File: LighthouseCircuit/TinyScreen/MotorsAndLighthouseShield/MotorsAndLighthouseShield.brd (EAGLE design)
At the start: 21.6 x 19.1 mm, 29 parts

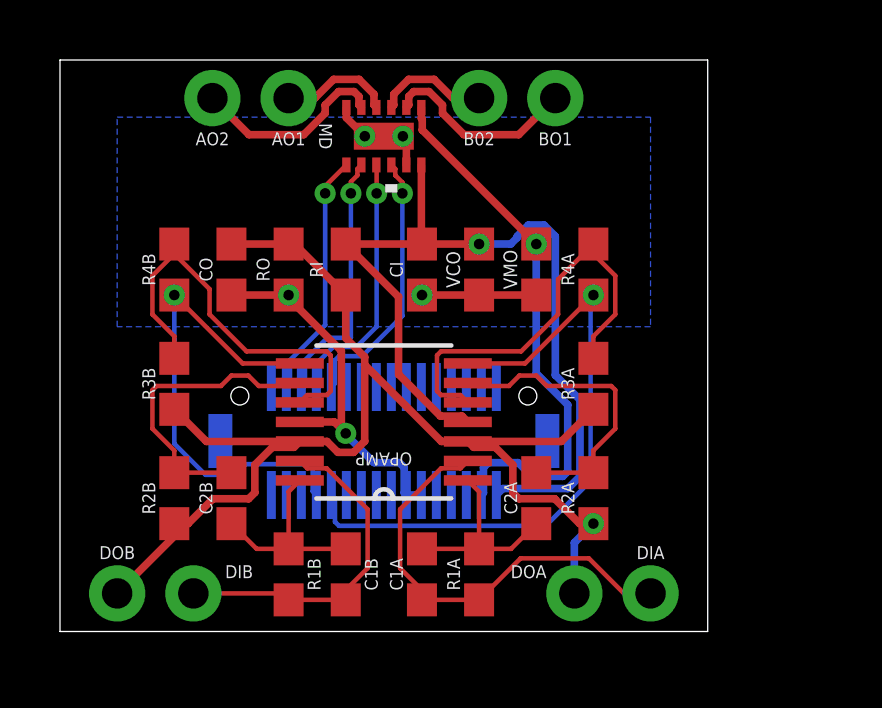
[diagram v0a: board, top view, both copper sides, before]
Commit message: Significantly stabilized the position calculation and the new driving model with independent PIDs for each wheel.
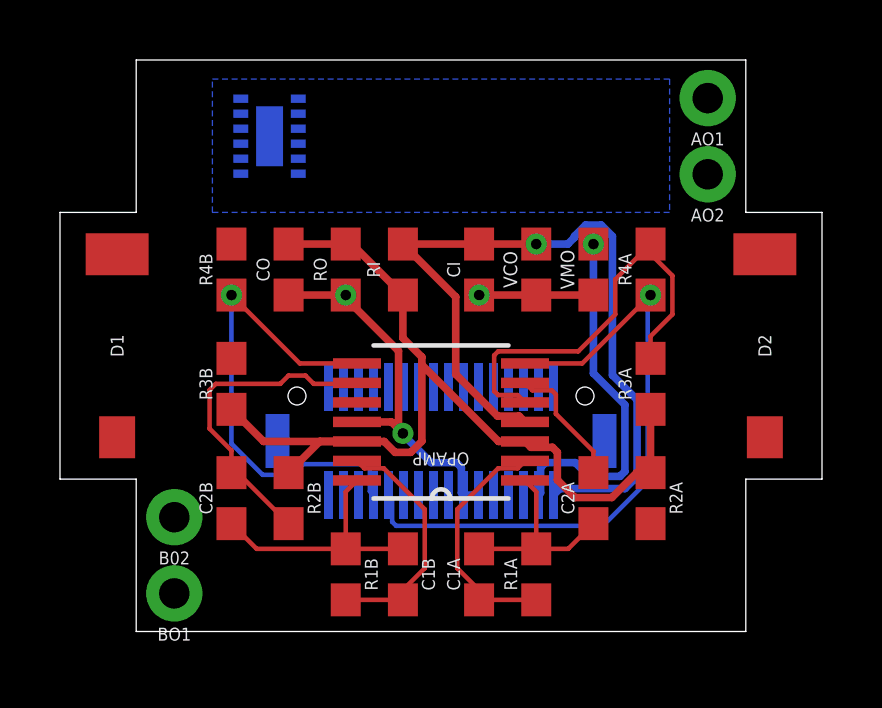
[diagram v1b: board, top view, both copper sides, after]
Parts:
- removed DIA, DIB, DOA, DOB: SINGLE-THROUGH-HOLE, ZippyComponentLibrary:SINGLE-THROUGH-HOLE
- added D1, D2: PHOTODIODEBPW, ZippyComponentLibrary:BPW34_BP104_SMD
- moved BO1 20.8 mm to (3.81, 1.27)
- moved B02 17.3 mm to (3.81, 3.81)
- moved AO2 16.7 mm to (21.6, 15.2)
- moved AO1 14.0 mm to (21.6, 17.8)
- moved R2B 3.81 mm to (7.62, 4.45), turned to 90 degrees
- moved MD 3.81 mm to (6.99, 16.5), flipped to the bottom, turned to 180 degrees
- moved C1A 1.91 mm to (14.0, 1.91)
- moved C2A 1.91 mm to (17.8, 4.45)
- moved CI 1.91 mm to (14.0, 12.1)
- moved VMO 1.91 mm to (17.8, 12.1)
- moved CO 1.91 mm to (7.62, 12.1)
- moved R1B 1.91 mm to (9.53, 1.91)
- moved RO 1.91 mm to (9.53, 12.1)
- moved R3B 1.90 mm to (5.71, 8.26)
- moved R4B 1.90 mm to (5.71, 12.1)
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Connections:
- net D1IN1: now also D2.CATHODE; no longer DIB.1
- net D2IN1: now also D1.CATHODE; no longer DIA.1
- net IO6: now also MD.10; no longer MD.7
- net IO7: now also MD.9; no longer MD.8
- net IO8: now also MD.8; no longer MD.9
- net IO9: now also MD.7; no longer MD.10
- net LVCC: now also D1.ANODE, D2.ANODE; no longer DOA.1, DOB.1
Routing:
- net N$11: track 14.2 -> 0.00 mm
- net LVCC: track 43.3 -> 31.9 mm, vias 1 -> 0
- net IO9: track 8.99 -> 0.00 mm, vias 1 -> 0
- net IO8: track 8.69 -> 0.00 mm, vias 1 -> 0
- net IO7: track 8.68 -> 0.00 mm, vias 1 -> 0
- net IO6: track 8.23 -> 0.00 mm, vias 1 -> 0
- net D2IN1: track 14.9 -> 8.15 mm
- net N$1: track 6.61 -> 0.00 mm
- net N$4: track 6.61 -> 0.00 mm
- net VBAT: track 18.2 -> 12.1 mm
- net D2OA2P1: track 10.3 -> 4.31 mm
- net N$2: track 3.78 -> 0.00 mm
- net N$3: track 3.78 -> 0.00 mm
- net GND: track 20.2 -> 16.7 mm, vias 5 -> 3
- net D1IN1: track 11.4 -> 8.15 mm
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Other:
- board size 21.6 x 19.1 mm -> 25.4 x 19.1 mm
